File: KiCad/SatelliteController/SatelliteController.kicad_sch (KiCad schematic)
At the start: 33 parts, among them J1 CONN_ICSP, J2 CONN_USB, J3 USB_B_Micro, U1 FT232RL, U2 ATMEGA2560-16AUR, Y1 HUSG-16.000-20

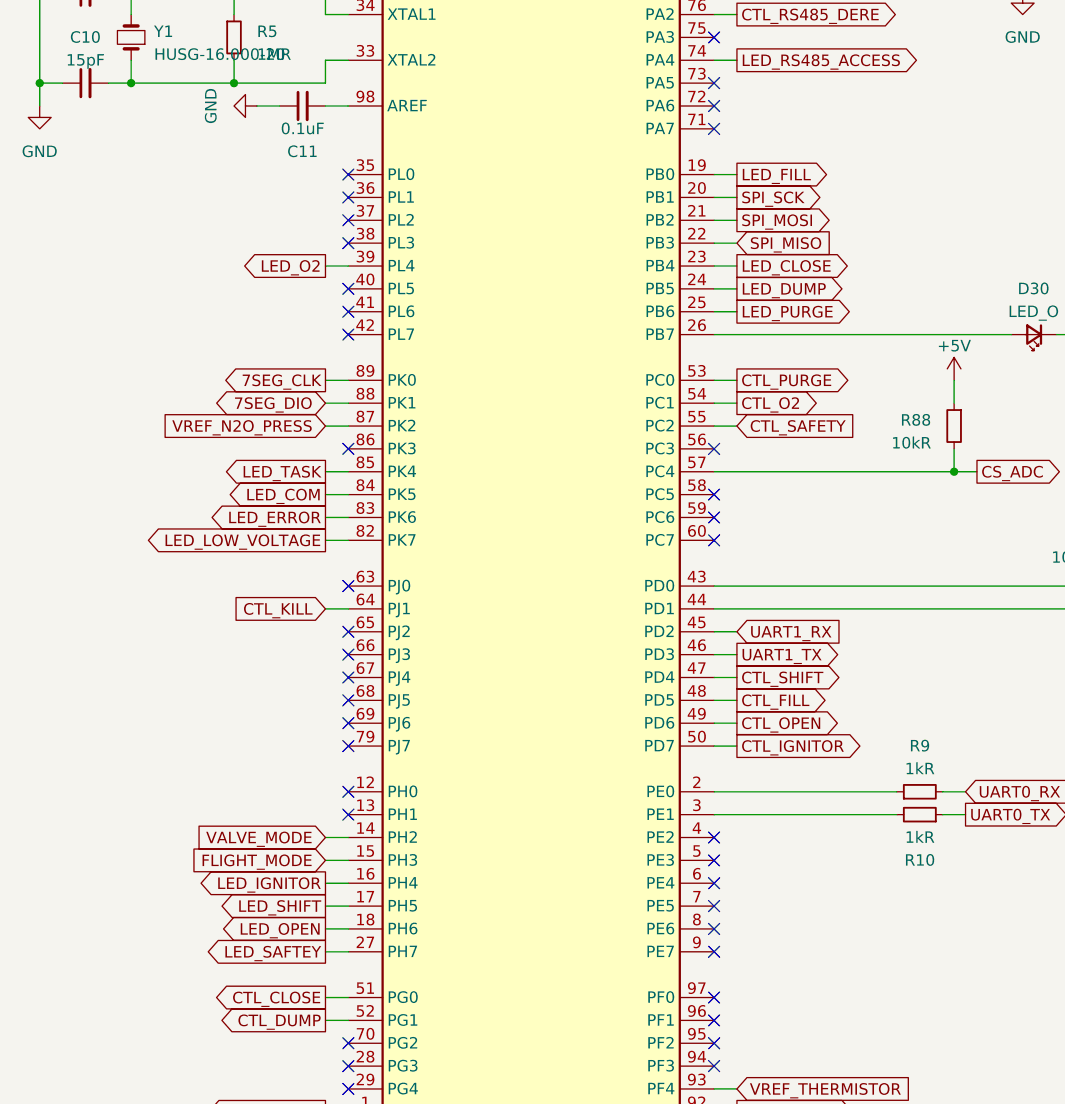
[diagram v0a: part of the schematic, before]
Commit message: サテコンの制御スイッチをプルダウンに変更
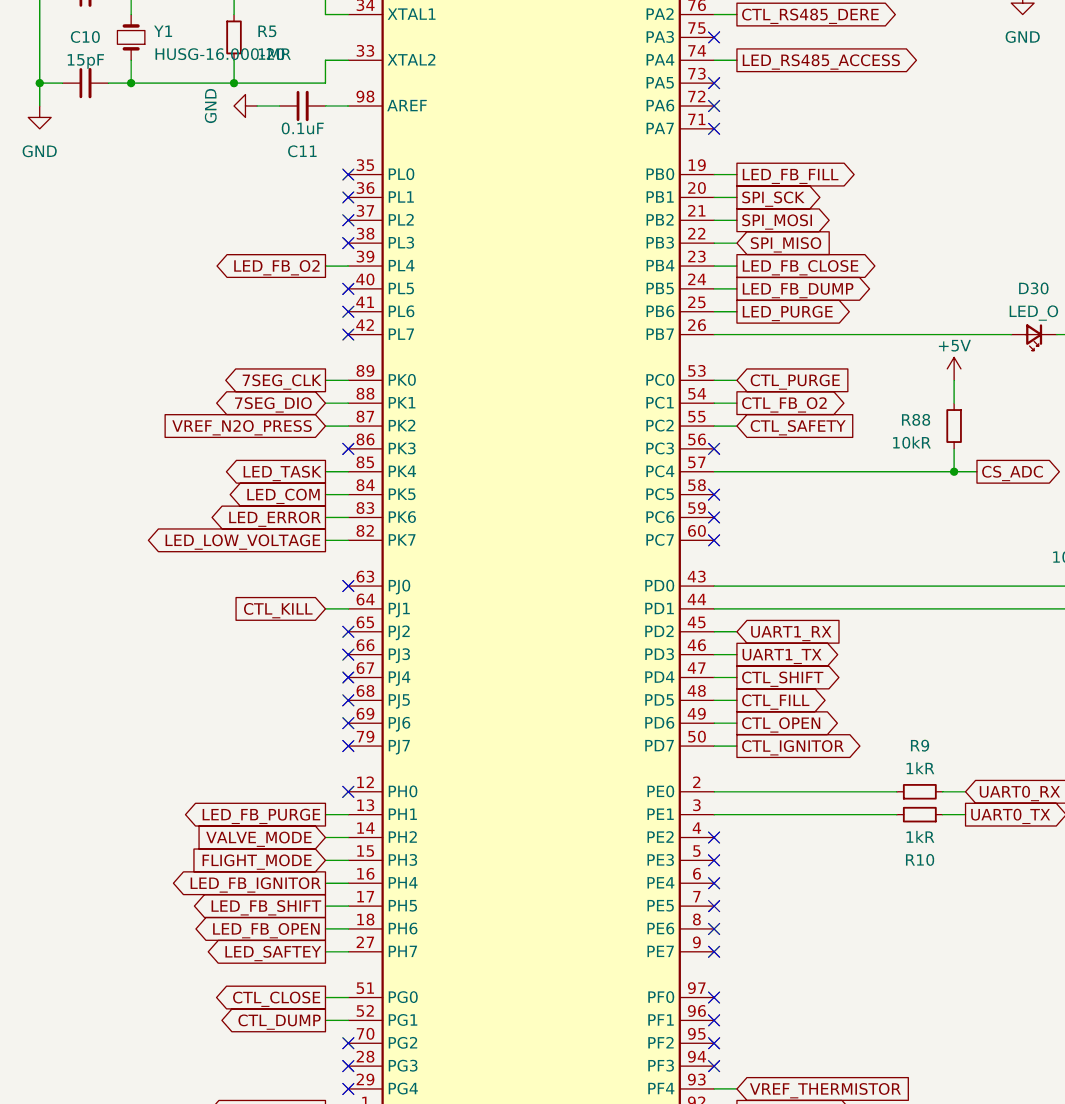
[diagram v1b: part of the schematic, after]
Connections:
- net LED_FB_PURGE: now reaches U2.13 (PH1)
- net CTL_O2 renamed CTL_FB_O2
- net LED_CLOSE renamed LED_FB_CLOSE
- net LED_DUMP renamed LED_FB_DUMP
- net LED_FILL renamed LED_FB_FILL
- net LED_IGNITOR renamed LED_FB_IGNITOR
- net LED_O2 renamed LED_FB_O2
- net LED_OPEN renamed LED_FB_OPEN
- net LED_SHIFT renamed LED_FB_SHIFT
- no-connect marks 54 -> 53
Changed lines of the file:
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@@
   (no_connect (at 95.25 177.8))
   (no_connect (at 54.61 172.72))
-  (no_connect (at 54.61 142.24))
   (no_connect (at 54.61 88.9))
   (wire (pts (xy 52.07 53.34) (xy 52.07 50.8))
@@
     (stroke (width 0) (type default))
   )
+  (wire (pts (xy 52.07 142.24) (xy 54.61 142.24))
+    (stroke (width 0) (type default))
+  )
   (wire (pts (xy 214.63 81.28) (xy 219.71 81.28))
     (stroke (width 0) (type default))
@@
     )
   )
-  (global_label "CTL_O2" (shape output) (at 97.79 96.52 0) (fields_autoplaced)
-    (effects (font (size 1.27 1.27)) (justify left))
-    (property "Intersheetrefs" "${INTERSHEET_REFS}" (at 107.4691 96.52 0)
+  (global_label "CTL_FB_O2" (shape output) (at 97.79 96.52 0) (fields_autoplaced)
+    (effects (font (size 1.27 1.27)) (justify left))
+    (property "Intersheetrefs" "${INTERSHEET_REFS}" (at 110.7953 96.52 0)
       (effects (font (size 1.27 1.27)) (justify left) hide)
     )
@@
     )
   )
-  (global_label "CTL_PURGE" (shape output) (at 97.79 93.98 0) (fields_autoplaced)
+  (global_label "CTL_PURGE" (shape input) (at 97.79 93.98 0) (fields_autoplaced)
     (effects (font (size 1.27 1.27)) (justify left))
     (property "Intersheetrefs" "${INTERSHEET_REFS}" (at 111.2186 93.98 0)
@@
     )
   )
-  (global_label "LED_SHIFT" (shape output) (at 52.07 152.4 180) (fields_autoplaced)
-    (effects (font (size 1.27 1.27)) (justify right))
-    (property "Intersheetrefs" "${INTERSHEET_REFS}" (at 39.5485 152.4 0)
+  (global_label "LED_FB_SHIFT" (shape output) (at 52.07 152.4 180) (fields_autoplaced)
+    (effects (font (size 1.27 1.27)) (justify right))
+    (property "Intersheetrefs" "${INTERSHEET_REFS}" (at 36.2223 152.4 0)
       (effects (font (size 1.27 1.27)) (justify right) hide)
     )
@@
     )
   )
-  (global_label "LED_FILL" (shape output) (at 97.79 71.12 0) (fields_autoplaced)
-    (effects (font (size 1.27 1.27)) (justify left))
-    (property "Intersheetrefs" "${INTERSHEET_REFS}" (at 108.8601 71.12 0)
+  (global_label "LED_FB_FILL" (shape output) (at 97.79 71.12 0) (fields_autoplaced)
+    (effects (font (size 1.27 1.27)) (justify left))
+    (property "Intersheetrefs" "${INTERSHEET_REFS}" (at 112.1863 71.12 0)
       (effects (font (size 1.27 1.27)) (justify left) hide)
     )
@@
     )
   )
-  (global_label "LED_DUMP" (shape output) (at 97.79 83.82 0) (fields_autoplaced)
-    (effects (font (size 1.27 1.27)) (justify left))
-    (property "Intersheetrefs" "${INTERSHEET_REFS}" (at 110.4324 83.82 0)
+  (global_label "LED_FB_DUMP" (shape output) (at 97.79 83.82 0) (fields_autoplaced)
+    (effects (font (size 1.27 1.27)) (justify left))
+    (property "Intersheetrefs" "${INTERSHEET_REFS}" (at 113.7586 83.82 0)
       (effects (font (size 1.27 1.27)) (justify left) hide)
     )
@@
     )
   )
+  (global_label "LED_FB_PURGE" (shape output) (at 52.07 142.24 180) (fields_autoplaced)
+    (effects (font (size 1.27 1.27)) (justify right))
+    (property "Intersheetrefs" "${INTERSHEET_REFS}" (at 35.1338 142.24 0)
+      (effects (font (size 1.27 1.27)) (justify right) hide)
+    )
+  )
   (global_label "UART1_RX" (shape input) (at 97.79 121.92 0) (fields_autoplaced)
     (effects (font (size 1.27 1.27)) (justify left))
@@
     )
   )
-  (global_label "LED_IGNITOR" (shape output) (at 52.07 149.86 180) (fields_autoplaced)
-    (effects (font (size 1.27 1.27)) (justify right))
-    (property "Intersheetrefs" "${INTERSHEET_REFS}" (at 37.3713 149.86 0)
-      (effects (font (size 1.27 1.27)) (justify right) hide)
-    )
-  )
-  (global_label "LED_OPEN" (shape output) (at 52.07 154.94 180) (fields_autoplaced)
-    (effects (font (size 1.27 1.27)) (justify right))
-    (property "Intersheetrefs" "${INTERSHEET_REFS}" (at 39.6695 154.94 0)
+  (global_label "LED_FB_IGNITOR" (shape output) (at 52.07 149.86 180) (fields_autoplaced)
+    (effects (font (size 1.27 1.27)) (justify right))
+    (property "Intersheetrefs" "${INTERSHEET_REFS}" (at 34.0451 149.86 0)
+      (effects (font (size 1.27 1.27)) (justify right) hide)
+    )
+  )
+  (global_label "LED_FB_OPEN" (shape output) (at 52.07 154.94 180) (fields_autoplaced)
+    (effects (font (size 1.27 1.27)) (justify right))
+    (property "Intersheetrefs" "${INTERSHEET_REFS}" (at 36.3433 154.94 0)
       (effects (font (size 1.27 1.27)) (justify right) hide)
     )
@@
     )
   )
-  (global_label "LED_O2" (shape output) (at 52.07 81.28 180) (fields_autoplaced)
-    (effects (font (size 1.27 1.27)) (justify right))
-    (property "Intersheetrefs" "${INTERSHEET_REFS}" (at 42.2095 81.28 0)
+  (global_label "LED_FB_O2" (shape output) (at 52.07 81.28 180) (fields_autoplaced)
+    (effects (font (size 1.27 1.27)) (justify right))
+    (property "Intersheetrefs" "${INTERSHEET_REFS}" (at 38.8833 81.28 0)
       (effects (font (size 1.27 1.27)) (justify right) hide)
     )
@@
     )
   )
-  (global_label "LED_CLOSE" (shape output) (at 97.79 81.28 0) (fields_autoplaced)
-    (effects (font (size 1.27 1.27)) (justify left))
-    (property "Intersheetrefs" "${INTERSHEET_REFS}" (at 111.0976 81.28 0)
-      (effects (font (size 1.27 1.27)) (justify left) hide)
-    )
+  (global_label "LED_FB_CLOSE" (shape output) (at 97.79 81.28 0) (fields_autoplaced)
+    (effects (font (size 1.27 1.27)) (justify left))
+    (property "Intersheetrefs" "${INTERSHEET_REFS}" (at 114.4238 81.28 0)
+      (effects (font (size 1.27 1.27)) (justify left) hide)
+    )

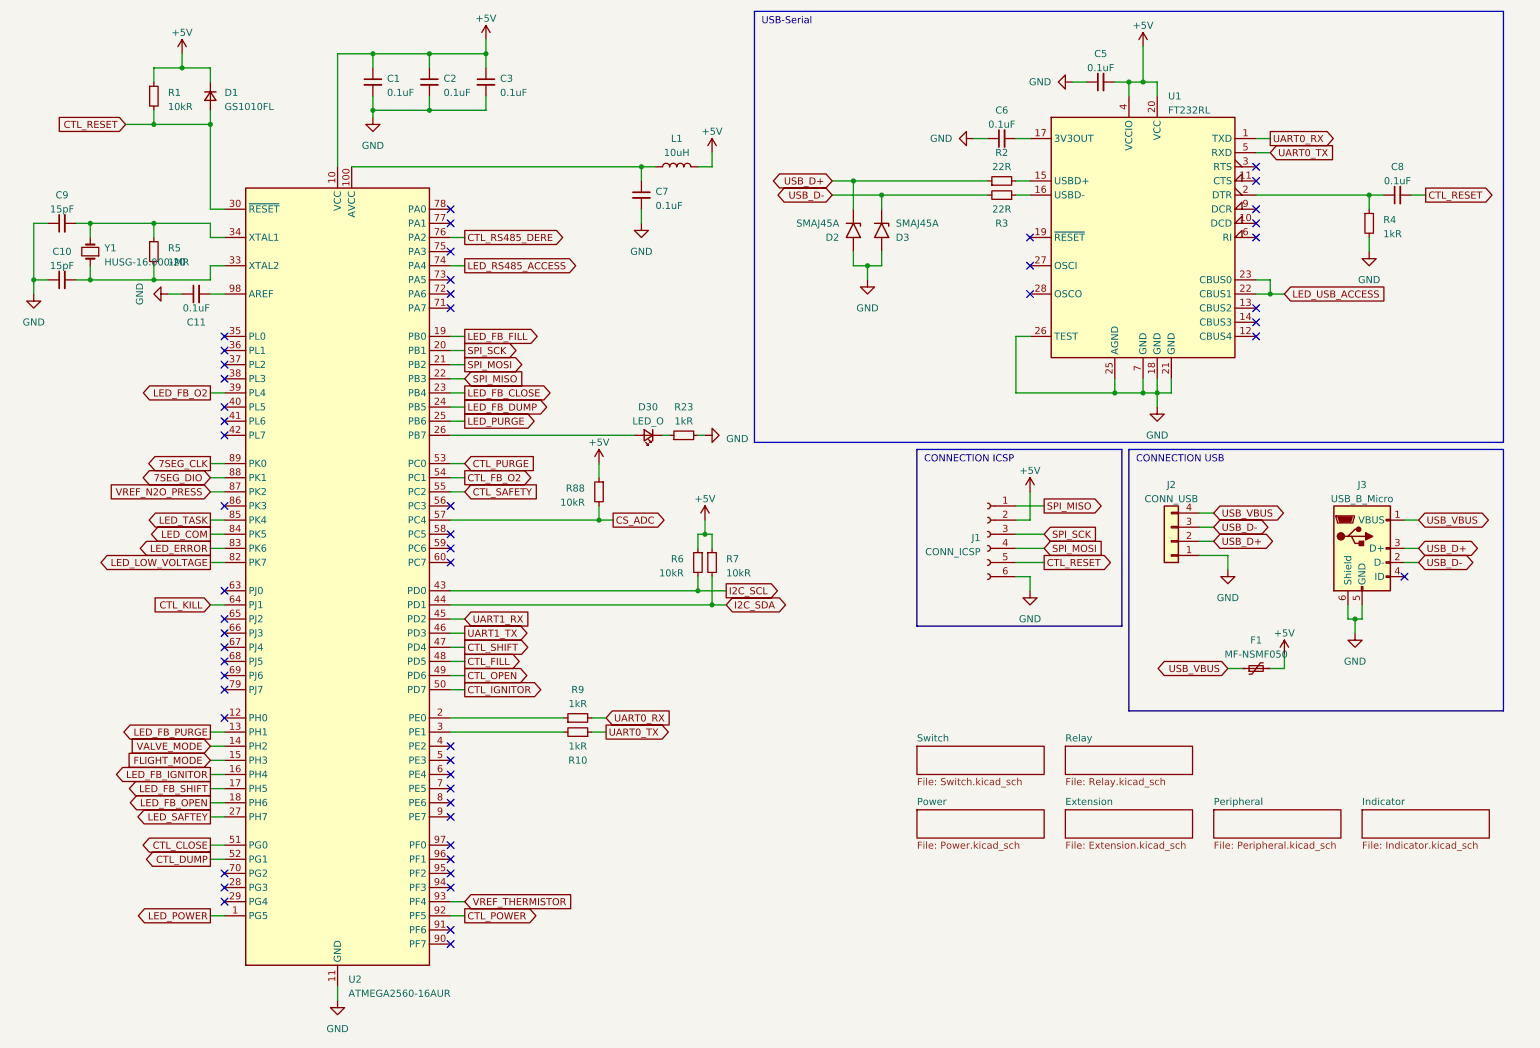
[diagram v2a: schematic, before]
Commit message: 電磁弁制御回路を整理
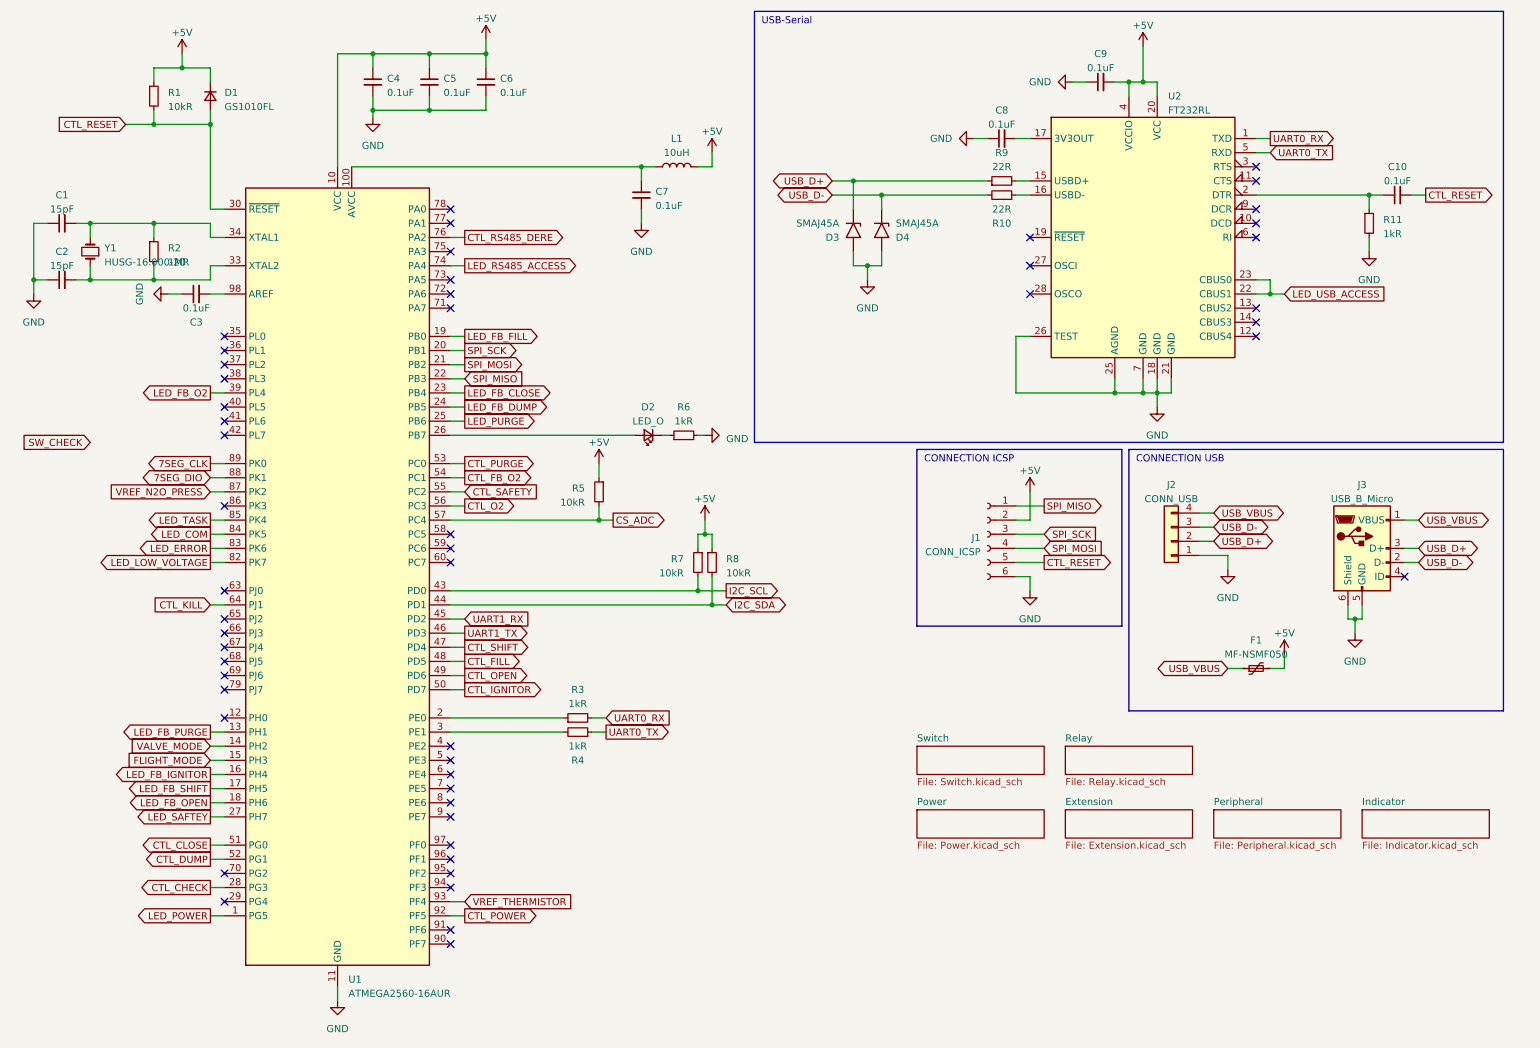
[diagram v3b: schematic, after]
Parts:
- renumbered C9 to C1, C8 to C10, C10 to C2, C11 to C3, C1 to C4, C2 to C5, C3 to C6, C6 to C8, C5 to C9, D30 to D2, D2 to D3, D3 to D4, R3 to R10, R4 to R11, R5 to R2, R9 to R3, R10 to R4, R88 to R5, R23 to R6, R6 to R7, R7 to R8, R2 to R9, U2 to U1, U1 to U2
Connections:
- net CTL_CHECK: now reaches U1.28 (PG3)
- net CTL_O2: now reaches U1.56 (PC3)
- no-connect marks 53 -> 51

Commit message: 配線
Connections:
- net SW_CHECK: now also U1.29 (PG4)
- no-connect marks 51 -> 50
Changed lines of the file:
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@@
-	)
-	(no_connect
-		(at 54.61 172.72)
 	)
 	(no_connect
@@
 		(pts
 			(xy 95.25 99.06) (xy 97.79 99.06)
+		)
+		(stroke
+			(width 0)
+			(type default)
+		)
+	)
+	(wire
+		(pts
+			(xy 52.07 172.72) (xy 54.61 172.72)
 		)
 		(stroke
@@
 	(global_label "SW_CHECK"
 		(shape input)
-		(at 30.48 90.17 180)
+		(at 52.07 172.72 180)
 		(fields_autoplaced yes)
 		(effects
@@
 		)
 		(property "Intersheetrefs" "${INTERSHEET_REFS}"
-			(at 17.5768 90.17 0)
+			(at 39.1668 172.72 0)
 			(effects
 				(font
